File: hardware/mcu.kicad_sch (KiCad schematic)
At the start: 35 parts, among them J5 Conn_ARM_JTAG_SWD_10, SW3 SW_Push, U2 EFR32FG28A122F1024GM48-A, U20 USBLC6-2P6, U21 USBLC6-2P6, X1 Crystal_GND2, Y1 Crystal

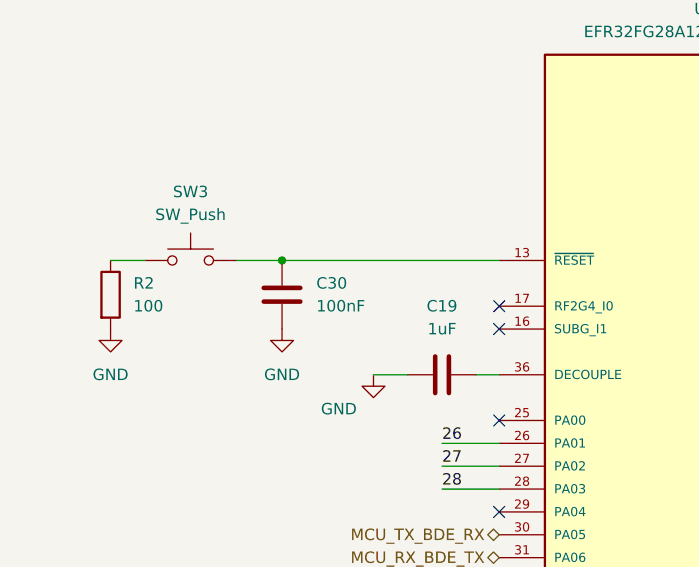
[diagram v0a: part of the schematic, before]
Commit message: MCU Reset Pin fix
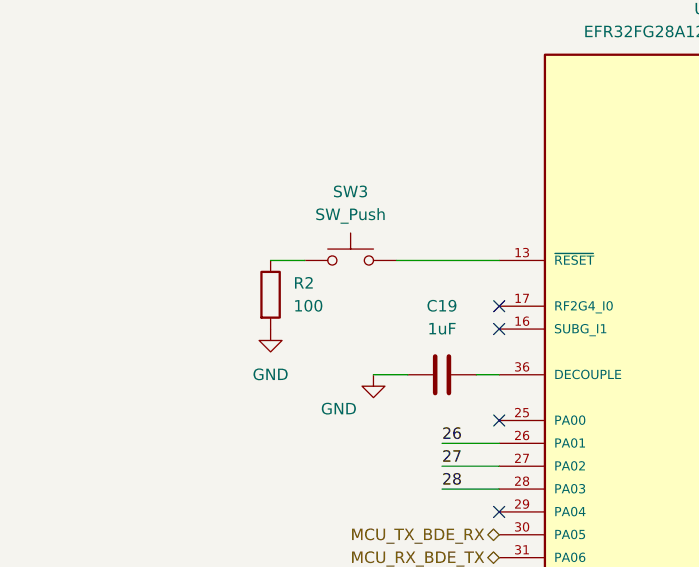
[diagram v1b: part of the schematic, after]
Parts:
- removed C30: 100nF, Capacitor_SMD:C_0402_1005Metric, symbol Device:C
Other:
- moved on the sheet: R2, SW3
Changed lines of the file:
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@@
 	)
 	(junction
-		(at 39.37 46.99)
-		(diameter 0)
-		(color 0 0 0 0)
-	)
-	(junction
 		(at 190.5 106.68)
 		(diameter 0)
@@
 	(wire
 		(pts
-			(xy 39.37 46.99) (xy 63.5 46.99)
-		)
-		(stroke
-			(width 0)
-			(type default)
-		)
-	)
-	(wire
-		(pts
 			(xy 132.08 62.23) (xy 115.57 62.23)
 		)
@@
 	(wire
 		(pts
-			(xy 20.32 46.99) (xy 24.13 46.99)
+			(xy 38.1 46.99) (xy 41.91 46.99)
 		)
 		(stroke
@@
 	(wire
 		(pts
-			(xy 34.29 46.99) (xy 39.37 46.99)
+			(xy 52.07 46.99) (xy 63.5 46.99)
 		)
 		(stroke
@@
 	(symbol
 		(lib_id "Switch:SW_Push")
-		(at 29.21 46.99 0)
+		(at 46.99 46.99 0)
 		(unit 1)
 		(exclude_from_sim no)
@@
 		(fields_autoplaced yes)
 		(property "Reference" "SW3"
-			(at 29.21 39.37 0)
+			(at 46.99 39.37 0)
 			(effects
 				(font
@@
 		)
 		(property "Value" "SW_Push"
-			(at 29.21 41.91 0)
+			(at 46.99 41.91 0)
 			(effects
 				(font
@@
 		)
 		(property "Footprint" "Button_Switch_SMD:SW_SPST_TL3305A"
-			(at 29.21 41.91 0)
+			(at 46.99 41.91 0)
 			(effects
 				(font
@@
 		)
 		(property "Datasheet" "~"
-			(at 29.21 41.91 0)
+			(at 46.99 41.91 0)
 			(effects
 				(font
@@
 		)
 		(property "Description" "Push button switch, generic, two pins"
-			(at 29.21 46.99 0)
+			(at 46.99 46.99 0)
 			(effects
 				(font
@@
 	(symbol
 		(lib_id "Device:R")
-		(at 20.32 50.8 0)
+		(at 38.1 50.8 0)
 		(unit 1)
 		(exclude_from_sim no)
@@
 		(fields_autoplaced yes)
 		(property "Reference" "R2"
-			(at 22.86 49.5299 0)
+			(at 40.64 49.5299 0)
 			(effects
 				(font
@@
 		)
 		(property "Value" "100"
-			(at 22.86 52.0699 0)
+			(at 40.64 52.0699 0)
 			(effects
 				(font
@@
 		)
 		(property "Footprint" "Resistor_SMD:R_0805_2012Metric"
-			(at 18.542 50.8 90)
+			(at 36.322 50.8 90)
 			(effects
 				(font
@@
 		)
 		(property "Datasheet" "~"
-			(at 20.32 50.8 0)
+			(at 38.1 50.8 0)
 			(effects
 				(font
@@
 		)
 		(property "Description" "Resistor"
-			(at 20.32 50.8 0)
+			(at 38.1 50.8 0)
 			(effects
 				(font
@@
 	)
 	(symbol
-		(lib_id "Device:C")
-		(at 39.37 50.8 0)
-		(unit 1)
-		(exclude_from_sim no)
-		(in_bom yes)
-		(on_board yes)
-		(dnp no)
-		(fields_autoplaced yes)
-		(property "Reference" "C30"
-			(at 43.18 49.5299 0)
-			(effects
-				(font
-					(size 1.27 1.27)
-				)
-				(justify left)
-			)
-		)
-		(property "Value" "100nF"
-			(at 43.18 52.0699 0)
-			(effects
-				(font
-					(size 1.27 1.27)
-				)
-				(justify left)
-			)
-		)
-		(property "Footprint" "Capacitor_SMD:C_0402_1005Metric"
-			(at 40.3352 54.61 0)
-			(effects
-				(font
-					(size 1.27 1.27)
-				)
-				(hide yes)
-			)
-		)
-		(property "Datasheet" "~"
-			(at 39.37 50.8 0)
-			(effects
-				(font
-					(size 1.27 1.27)
-				)
-				(hide yes)
-			)
-		)
-		(property "Description" "Unpolarized capacitor"
-			(at 39.37 50.8 0)
-			(effects
-				(font
-					(size 1.27 1.27)
-				)
-				(hide yes)
-			)
-		)
-		(pin "2"
-		)
-		(pin "1"
-		)
-		(instances
-			(project "Senior_Design"
-				(path "/8f5928e8-0fc1-4443-a20f-3bfeb956761e/eaf224bf-a12f-4d12-aa0a-28551b47d007"
-					(reference "C30")
-					(unit 1)
-				)
-			)
-		)
-	)
-	(symbol
 		(lib_id "Power_Protection:USBLC6-2P6")
 		(at 101.6 166.37 0)
@@
 	(symbol
 		(lib_id "power:GND")
-		(at 20.32 54.61 0)
+		(at 38.1 54.61 0)
 		(unit 1)
 		(exclude_from_sim no)
@@
 		(fields_autoplaced yes)
 		(property "Reference" "#PWR012"
-			(at 20.32 60.96 0)
+			(at 38.1 60.96 0)
 			(effects
 				(font
@@
 		)
 		(property "Value" "GND"
-			(at 20.32 59.69 0)
+			(at 38.1 59.69 0)
 			(effects
 				(font
@@
 		)
 		(property "Footprint" ""
-			(at 20.32 54.61 0)
+			(at 38.1 54.61 0)
 			(effects
 				(font
@@
 		)
 		(property "Datasheet" ""
-			(at 20.32 54.61 0)
+			(at 38.1 54.61 0)
 			(effects
 				(font
@@
 		)
 		(property "Description" "Power symbol creates a global label with name \"GND\" , ground"
-			(at 20.32 54.61 0)
+			(at 38.1 54.61 0)
 			(effects
 				(font
@@
 					(unit 1)
 				)
-			)
-		)
-	)
-	(symbol
-		(lib_id "power:GND")
-		(at 39.37 54.61 0)
-		(unit 1)
-		(exclude_from_sim no)
-		(in_bom yes)
-		(on_board yes)
-		(dnp no)
-		(fields_autoplaced yes)
-		(property "Reference" "#PWR013"
-			(at 39.37 60.96 0)
-			(effects
-				(font
-					(size 1.27 1.27)
-				)
-				(hide yes)
-			)
-		)
-		(property "Value" "GND"
-			(at 39.37 59.69 0)
-			(effects
-				(font
-					(size 1.27 1.27)
-				)
-			)
-		)
-		(property "Footprint" ""
-			(at 39.37 54.61 0)
-			(effects
-				(font
-					(size 1.27 1.27)
-				)
-				(hide yes)
-			)
-		)
-		(property "Datasheet" ""
-			(at 39.37 54.61 0)
-			(effects
-				(font
-					(size 1.27 1.27)
-				)
-				(hide yes)
-			)
-		)
-		(property "Description" "Power symbol creates a global label with name \"GND\" , ground"
-			(at 39.37 54.61 0)
-			(effects
-				(font
-					(size 1.27 1.27)
-				)
-				(hide yes)
-			)
-		)
-		(pin "1"
-		)
-		(instances
-			(project "Senior_Design"
-				(path "/8f5928e8-0fc1-4443-a20f-3bfeb956761e/eaf224bf-a12f-4d12-aa0a-28551b47d007"
-					(reference "#PWR013")
-					(unit 1)
-				)

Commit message: test
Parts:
- X1: value Crystal_GND2 -> HF_Crystal
- Y1: value Crystal -> LF_Crystal
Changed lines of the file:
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@@
 			)
 		)
-		(property "Value" "Crystal_GND2"
+		(property "Value" "HF_Crystal"
 			(at 132.08 104.902 90)
 			(effects
@@
 			)
 		)
-		(property "Value" "Crystal"
+		(property "Value" "LF_Crystal"
 			(at 124.46 90.1699 90)
 			(effects

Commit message: MCU Capacitor Updates
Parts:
- removed C24, C31, C32: 0.1uF, Capacitor_SMD:C_0402_1005Metric, symbol Device:C
- removed C33, C37: 1uF, Capacitor_SMD:C_0402_1005Metric, symbol Device:C
- removed C35: 120pF, Capacitor_SMD:C_0402_1005Metric, symbol Device:C
- removed C36: 100nF, Capacitor_SMD:C_0402_1005Metric, symbol Device:C
- removed C87: 4.7uF, Capacitor_SMD:C_0402_1005Metric, symbol Device:C
- removed FB1: BLM03AG700SN1, Resistor_SMD:R_0201_0603Metric, symbol Device:FerriteBead
- removed FB2: BLM03PG330SN1, Resistor_SMD:R_0603_1608Metric, symbol Device:FerriteBead
- removed L3: 2.2uH, Inductor_SMD:L_7.3x7.3_H3.5, symbol Device:L
- C16: value 10uF -> 0.1uF; footprint Capacitor_SMD:C_0402_1005Metric -> (none)
- C20: value 10nF -> 2.7uF; footprint Capacitor_SMD:C_0402_1005Metric -> (none)
- C21: value 100nF -> 1uF; footprint Capacitor_SMD:C_0402_1005Metric -> (none)
- C22: value 120pF -> 0.1uF; footprint Capacitor_SMD:C_0402_1005Metric -> (none)
- C23: value 1uF -> 10nF; footprint Capacitor_SMD:C_0402_1005Metric -> (none)
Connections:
- net DVDD is gone; now on net BUCK_3.3V: U2.14 (RFVDD), U2.20 (PAVDD), U2.40 (DVDD)
- net PAVDD is gone; now on net BUCK_3.3V: C21.1, C22.1
- net VREGSW: no longer names the net of U2.37 (VREGSW)
- no-connect marks 12 -> 13

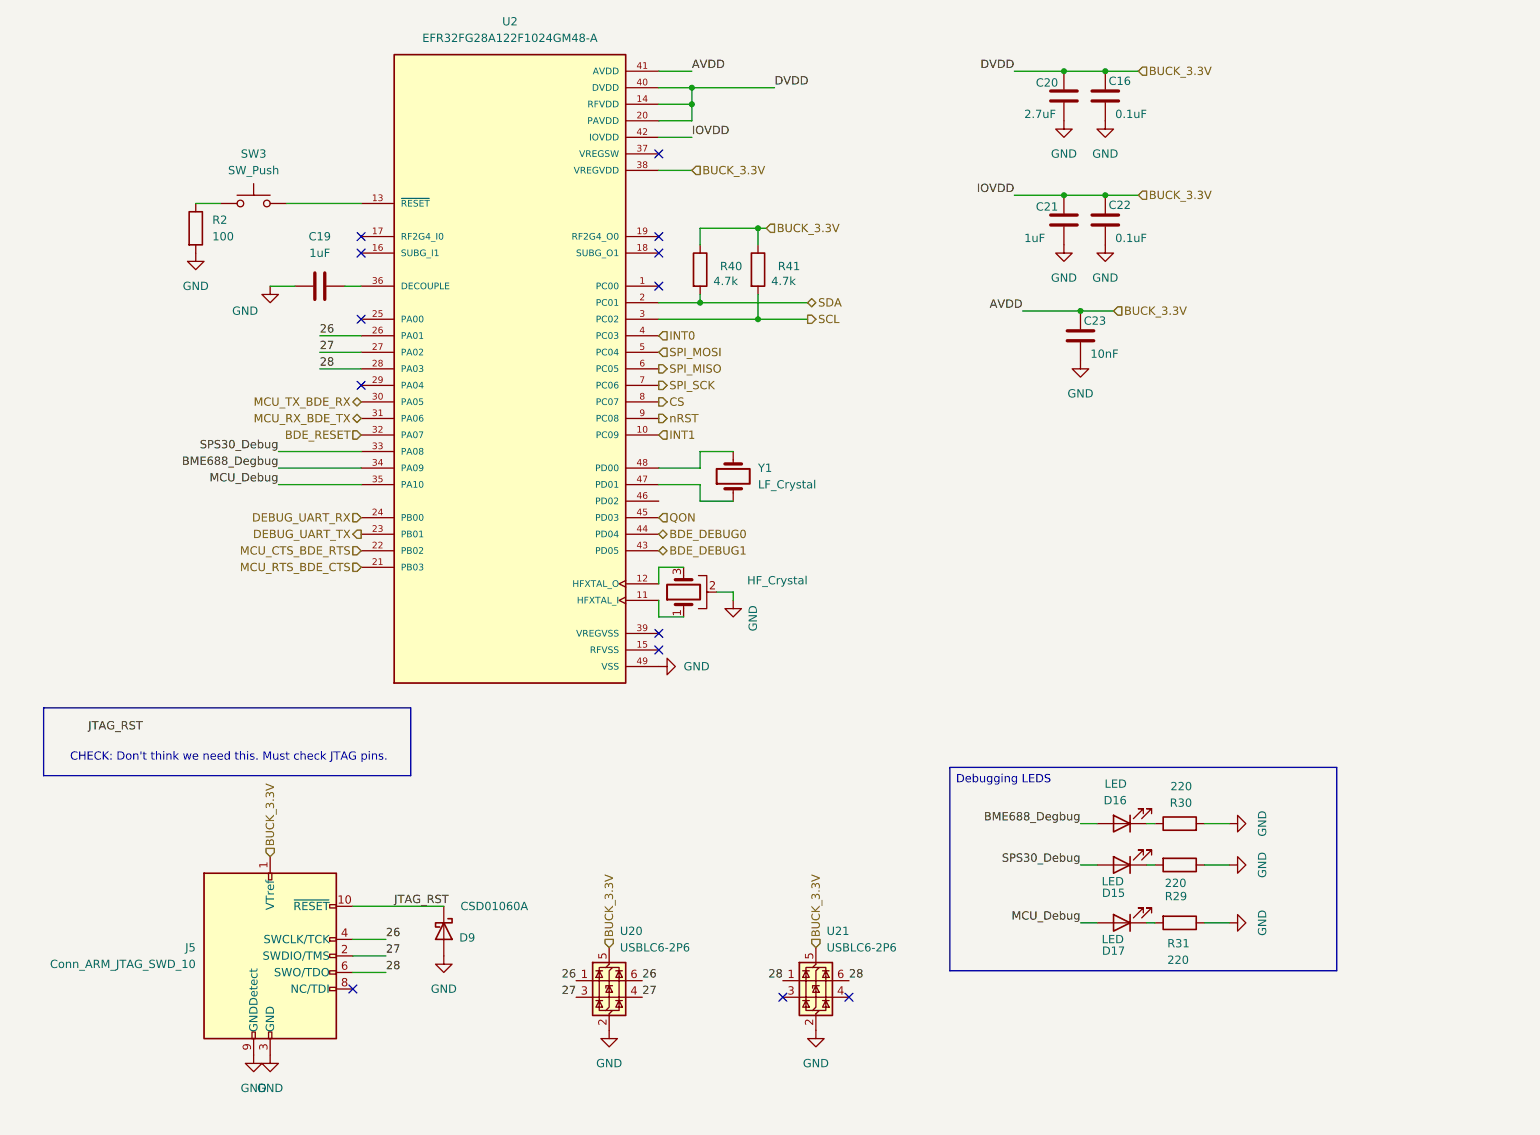
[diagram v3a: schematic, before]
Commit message: Fixed MCU JTAG/Reordered pages
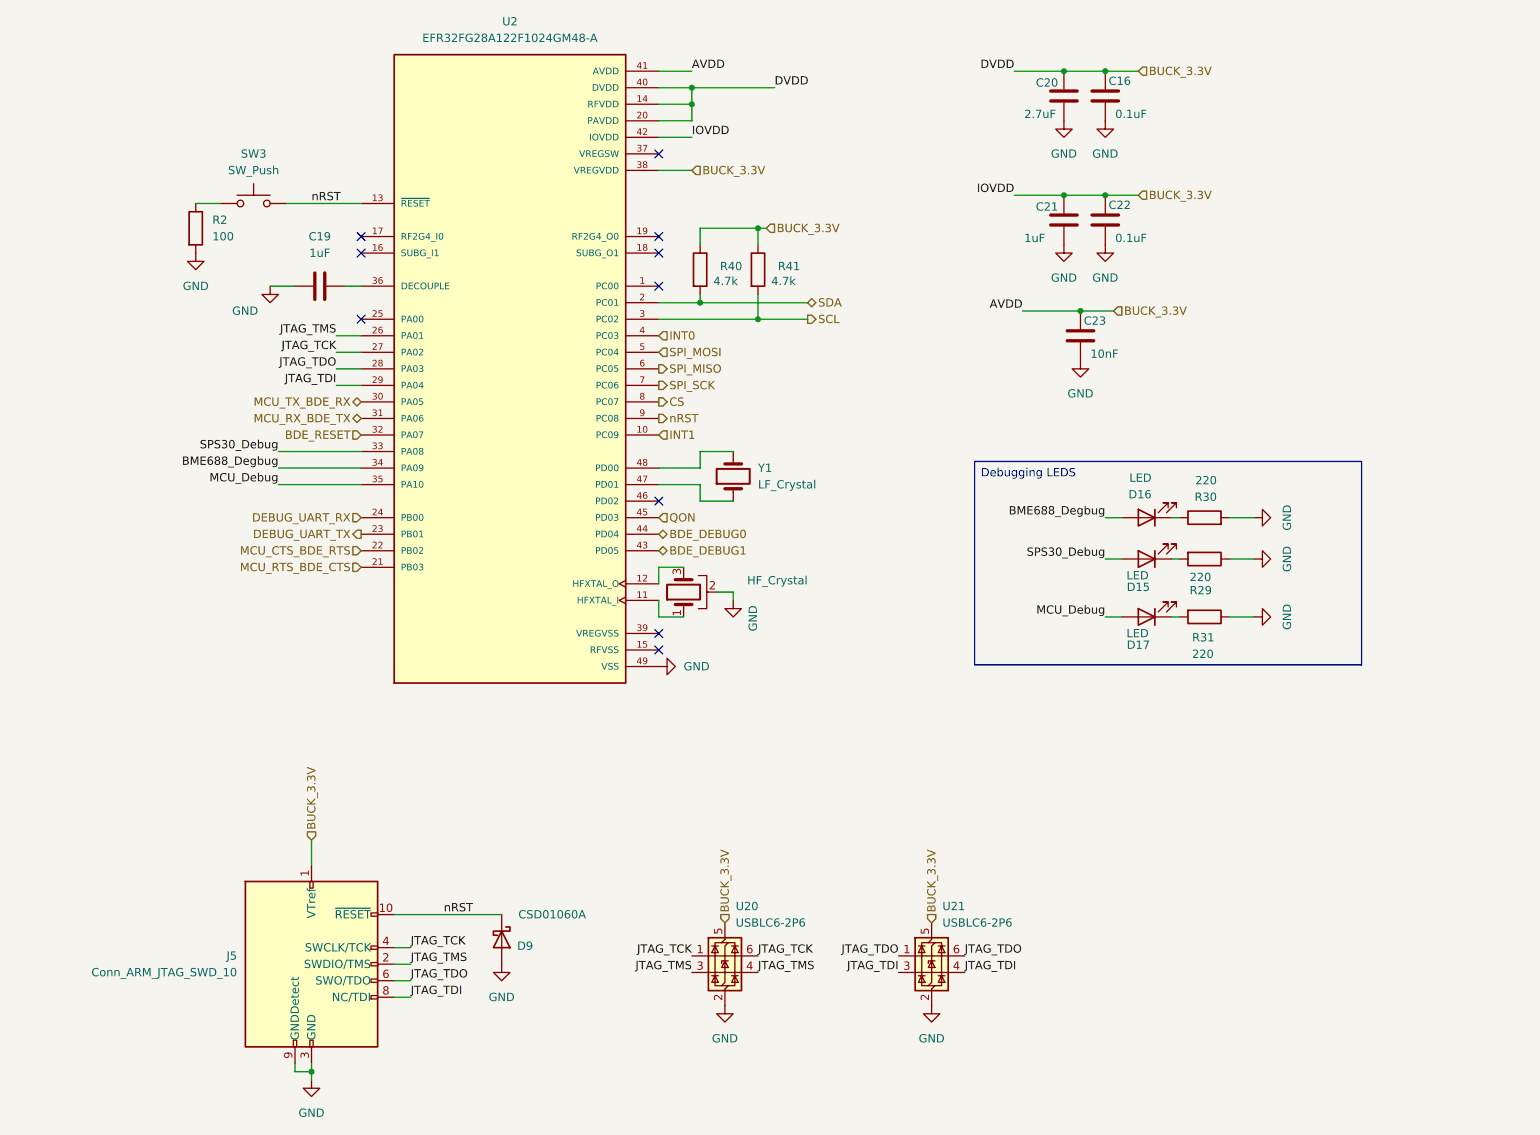
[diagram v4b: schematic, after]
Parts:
- J5: footprint Connector_PinHeader_1.27mm:PinHeader_2x05_P1.27mm_Vertical -> Connector_PinHeader_1.27mm:PinHeader_2x05_P1.27mm_Vertical_SMD
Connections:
- net JTAG_RST is gone; now on net nRST: D9.1 (K), J5.10 (~{RESET})
- net nRST: now also SW3.2, U2.13 (~{RESET})
- net JTAG_TDI: now reaches U2.29 (PA04)
- net JTAG_TDI: now also J5.8 (NC/TDI), U21.3 (I/O2), U21.4 (I/O2)
- net 26 renamed JTAG_TCK
- net JTAG_TCK: now also U2.27 (PA02); no longer U2.26 (PA01)
- net 27 renamed JTAG_TMS
- net JTAG_TMS: now also U2.26 (PA01); no longer U2.27 (PA02)
- net 28 renamed JTAG_TDO
- no-connect marks 13 -> 10
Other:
- note removed: "CHECK: Don't think we need this. Must check JTAG pins."
- moved on the sheet: D15, D16, D17, D9, J5, R29, R30, R31, U20, U21

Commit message: Fixed MCU power pins
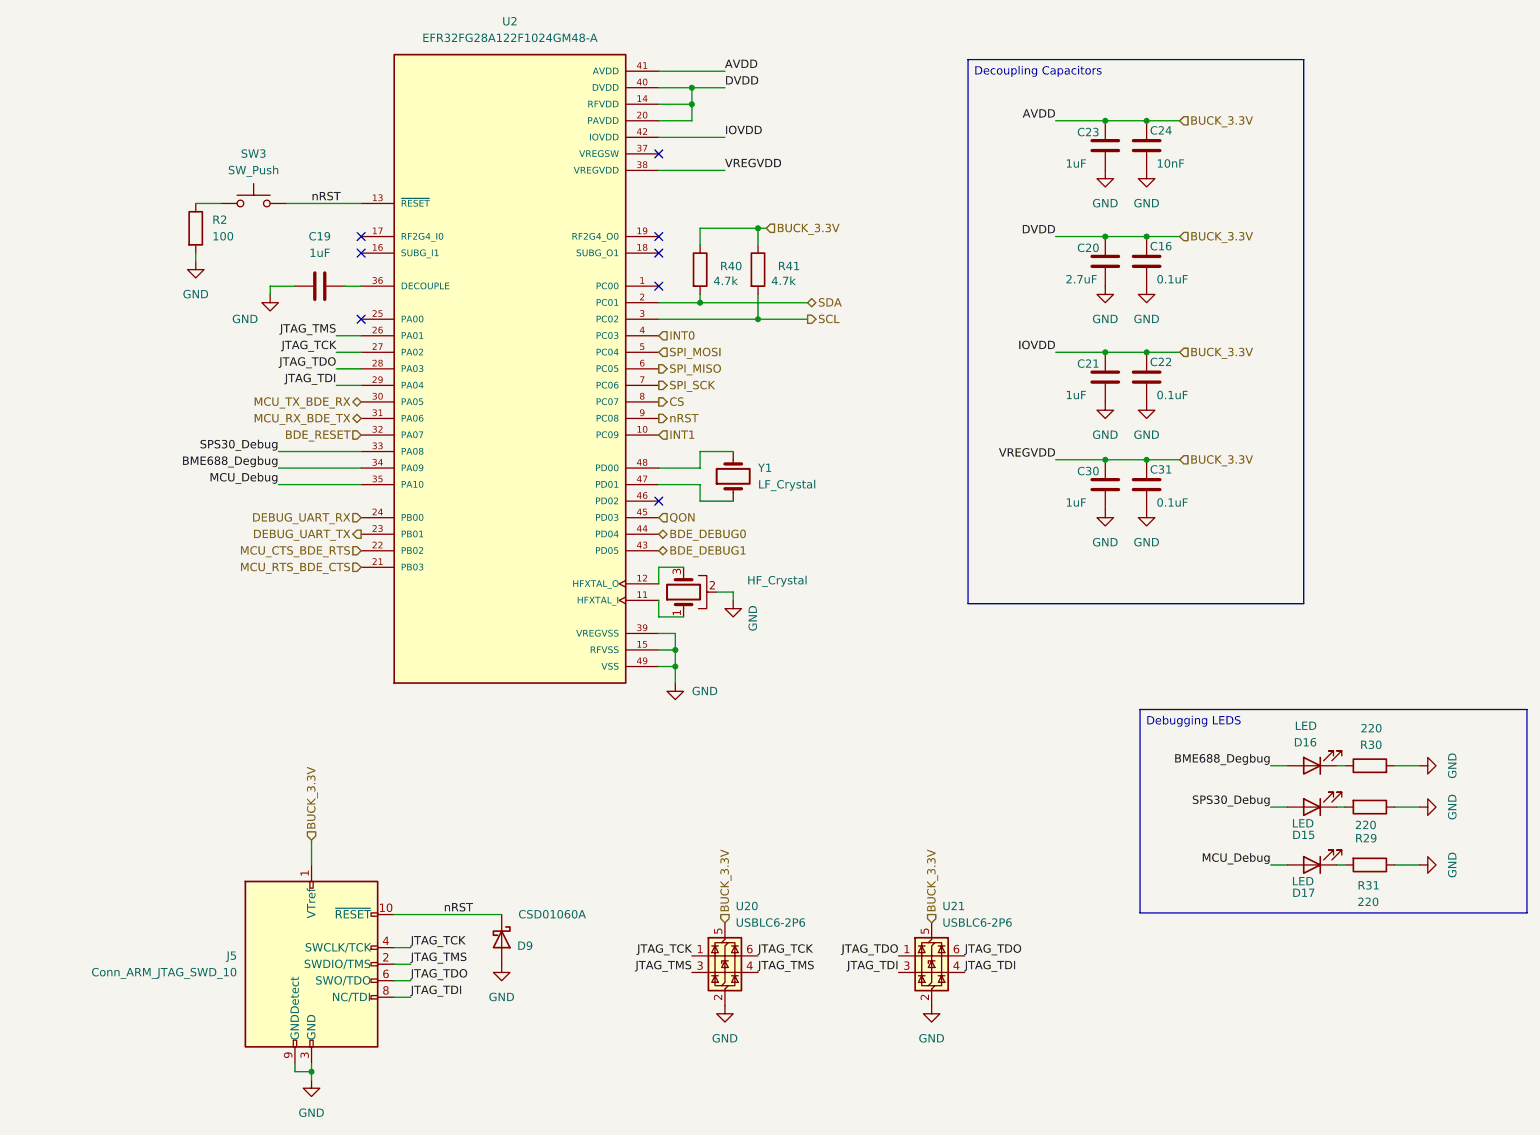
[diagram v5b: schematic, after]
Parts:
- added C24: 10nF, symbol Device:C
- added C30: 1uF, symbol Device:C
- added C31: 0.1uF, symbol Device:C
- C23: value 10nF -> 1uF
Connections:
- net BUCK_3.3V: now also C24.1, C30.1, C31.1
- net GND: now also U2.15 (RFVSS), U2.39 (VREGVSS), C24.2, C30.2, C31.2
- no-connect marks 10 -> 8
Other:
- moved on the sheet: C16, C20, C21, C22, D15, D16, D17, R29, R30, R31
